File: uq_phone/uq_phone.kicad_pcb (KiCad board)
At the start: 4 copper layers, 42.8 x 103.8 mm, 145 parts, among them J1 USB4105-GF-A, J10 SJ-3551B-MSMT-TR-67, J11 Conn_01x02, J2 S3B-PH-SM4-TB_LF__SN_, J3 20279-001E-03, J4 20279-001E-03, J5 FI-RE51S-HF-R1500, J6 Conn_ARM_SWD_TagConnect_TC2030, J7 Conn_01x02, J8 KP15B-6S-SF_800_, M1 VCDM0834B004L, Q1 MMBT3904LP-7, Q2 MMBT3904LP-7, U1 MCP73871-2CCI_ML, U10 TPD3F303DQDR, U11 TPD8F003DQDR, U12 MCP1664T-E/OT, U13 TS3A5018RSVR, U14 NAU88C22YG, U2 TPS62162DSGR, U3 BQ27441DRZR-G1A, U4 RC7620_1104625, U5 TXB0108RGYR, U6 TXB0108RGYR, U7 STM32H733VGTx, U8 LSM6DSVTR, U9 DRV2603RUNR

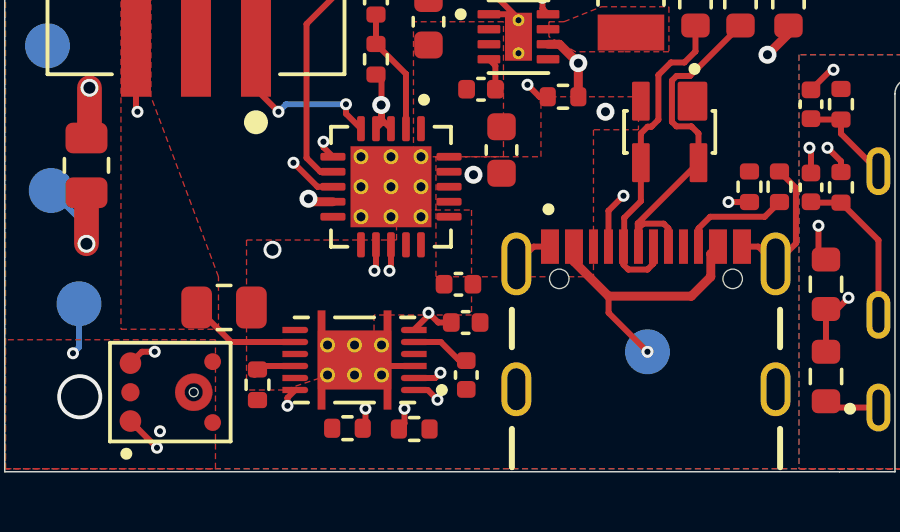
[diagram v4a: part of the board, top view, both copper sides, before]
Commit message: Clean up and add DNP
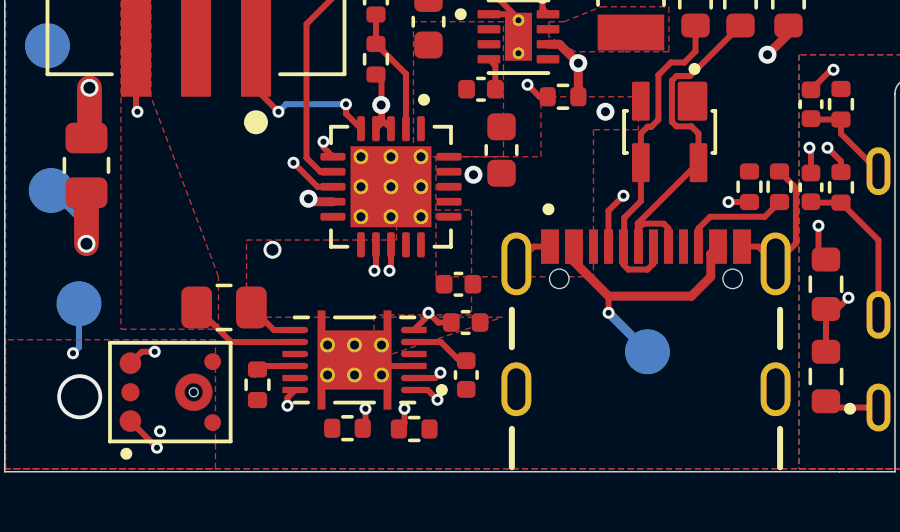
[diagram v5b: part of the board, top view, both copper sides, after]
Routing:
- net VBAT: track 10.2 -> 12.0 mm
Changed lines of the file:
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@@
 		(net 7)
 	)
+	(segment
+		(start 36.3475 167.275)
+		(end 37.06 167.275)
+		(width 0.2)
+		(layer "F.Cu")
+		(net 7)
+	)
+	(segment
+		(start 35.5975 166.525)
+		(end 36.3475 167.275)
+		(width 0.2)
+		(layer "F.Cu")
+		(net 7)
+	)
 	(via
 		(at 30.1 164.4)
@@
 	)
 	(segment
-		(start 47.503319 166.147002)
-		(end 47.503319 166.703319)
-		(width 0.2)
-		(layer "F.Cu")
-		(net 8)
-	)
-	(segment
 		(start 53.5 157.125)
 		(end 53.5 157.4)
@@
 	(segment
 		(start 47.503319 166.703319)
-		(end 48.8 168)
+		(end 47.503319 166.147002)
 		(width 0.2)
 		(layer "F.Cu")
@@
 	)
 	(via
-		(at 48.8 168)
+		(at 47.503319 166.703319)
 		(size 0.4)
 		(drill 0.2)
@@
 	)
 	(segment
+		(start 48.8 168)
+		(end 47.503319 166.703319)
+		(width 0.3)
+		(layer "B.Cu")
+		(net 8)
+	)
+	(segment
 		(start 52.8 158.1)
 		(end 50.9 160)
@@
 		(polygon
 			(pts
-				(xy 42.935 163.275) (xy 42.935 166.775) (xy 39.685 166.775) (xy 39.685 168.275) (xy 36.685 169.275)
-				(xy 35.435 169.275) (xy 35.435 164.275) (xy 40.435 164.275) (xy 40.435 163.275)
+				(xy 42.935 163.275) (xy 42.935 166.775) (xy 39.685 166.775) (xy 39.685 168.275) (xy 43.96 166.85)
+				(xy 35.435 166.85) (xy 35.435 164.275) (xy 40.435 164.275) (xy 40.435 163.275)
 			)
 		)
